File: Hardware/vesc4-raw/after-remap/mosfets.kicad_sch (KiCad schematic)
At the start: 15 parts, among them Q1 IRFS7530, Q2 IRFS7530, Q3 IRFS7530, Q4 IRFS7530, Q5 IRFS7530, Q6 IRFS7530

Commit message: export footprint & ngapus warning unmatched
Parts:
- Q1: symbol after-remap-rescue:MOSFET_N -> vesc4-legacy:MOSFET_N_8
- Q2: symbol after-remap-rescue:MOSFET_N -> vesc4-legacy:MOSFET_N_7
- Q3: symbol after-remap-rescue:MOSFET_N -> vesc4-legacy:MOSFET_N_11
- Q4: symbol after-remap-rescue:MOSFET_N -> vesc4-legacy:MOSFET_N_10
- Q5: symbol after-remap-rescue:MOSFET_N -> vesc4-legacy:MOSFET_N_12
- Q6: symbol after-remap-rescue:MOSFET_N -> vesc4-legacy:MOSFET_N_9
- R28: symbol after-remap-rescue:R-RESCUE-BLDC_4 -> vesc4-legacy:R-RESCUE-BLDC_4_13
- R29: symbol after-remap-rescue:R-RESCUE-BLDC_4 -> vesc4-legacy:R-RESCUE-BLDC_4_11
- R30: symbol after-remap-rescue:R-RESCUE-BLDC_4 -> vesc4-legacy:R-RESCUE-BLDC_4_10
- R34: symbol after-remap-rescue:R-RESCUE-BLDC_4 -> vesc4-legacy:R-RESCUE-BLDC_4_12
- R35: symbol after-remap-rescue:R-RESCUE-BLDC_4 -> vesc4-legacy:R-RESCUE-BLDC_4_15
- R36: symbol after-remap-rescue:R-RESCUE-BLDC_4 -> vesc4-legacy:R-RESCUE-BLDC_4_14
- R42: symbol after-remap-rescue:R-RESCUE-BLDC_4 -> vesc4-legacy:R-RESCUE-BLDC_4_18
- R43: symbol after-remap-rescue:R-RESCUE-BLDC_4 -> vesc4-legacy:R-RESCUE-BLDC_4_16
- R46: symbol after-remap-rescue:R-RESCUE-BLDC_4 -> vesc4-legacy:R-RESCUE-BLDC_4_17
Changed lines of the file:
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@@
 	(symbol
 		(lib_name "R-RESCUE-BLDC_4_17")
-		(lib_id "after-remap-rescue:R-RESCUE-BLDC_4")
+		(lib_id "vesc4-legacy:R-RESCUE-BLDC_4_17")
 		(at 199.39 102.87 270)
 		(unit 1)
@@
 	(symbol
 		(lib_name "R-RESCUE-BLDC_4_10")
-		(lib_id "after-remap-rescue:R-RESCUE-BLDC_4")
+		(lib_id "vesc4-legacy:R-RESCUE-BLDC_4_10")
 		(at 119.38 102.87 270)
 		(unit 1)
@@
 	(symbol
 		(lib_name "MOSFET_N_8")
-		(lib_id "after-remap-rescue:MOSFET_N")
+		(lib_id "vesc4-legacy:MOSFET_N_8")
 		(at 125.73 71.12 0)
 		(unit 1)
@@
 	(symbol
 		(lib_name "MOSFET_N_7")
-		(lib_id "after-remap-rescue:MOSFET_N")
+		(lib_id "vesc4-legacy:MOSFET_N_7")
 		(at 125.73 95.25 0)
 		(unit 1)
@@
 	(symbol
 		(lib_name "R-RESCUE-BLDC_4_11")
-		(lib_id "after-remap-rescue:R-RESCUE-BLDC_4")
+		(lib_id "vesc4-legacy:R-RESCUE-BLDC_4_11")
 		(at 111.76 95.25 270)
 		(unit 1)
@@
 	(symbol
 		(lib_name "R-RESCUE-BLDC_4_13")
-		(lib_id "after-remap-rescue:R-RESCUE-BLDC_4")
+		(lib_id "vesc4-legacy:R-RESCUE-BLDC_4_13")
 		(at 111.76 71.12 270)
 		(unit 1)
@@
 	(symbol
 		(lib_name "R-RESCUE-BLDC_4_12")
-		(lib_id "after-remap-rescue:R-RESCUE-BLDC_4")
+		(lib_id "vesc4-legacy:R-RESCUE-BLDC_4_12")
 		(at 151.13 71.12 270)
 		(unit 1)
@@
 	(symbol
 		(lib_name "R-RESCUE-BLDC_4_15")
-		(lib_id "after-remap-rescue:R-RESCUE-BLDC_4")
+		(lib_id "vesc4-legacy:R-RESCUE-BLDC_4_15")
 		(at 151.13 95.25 270)
 		(unit 1)
@@
 	(symbol
 		(lib_name "MOSFET_N_10")
-		(lib_id "after-remap-rescue:MOSFET_N")
+		(lib_id "vesc4-legacy:MOSFET_N_10")
 		(at 165.1 95.25 0)
 		(unit 1)
@@
 	(symbol
 		(lib_name "MOSFET_N_11")
-		(lib_id "after-remap-rescue:MOSFET_N")
+		(lib_id "vesc4-legacy:MOSFET_N_11")
 		(at 165.1 71.12 0)
 		(unit 1)
@@
 	(symbol
 		(lib_name "MOSFET_N_12")
-		(lib_id "after-remap-rescue:MOSFET_N")
+		(lib_id "vesc4-legacy:MOSFET_N_12")
 		(at 205.74 71.12 0)
 		(unit 1)
@@
 	(symbol
 		(lib_name "MOSFET_N_9")
-		(lib_id "after-remap-rescue:MOSFET_N")
+		(lib_id "vesc4-legacy:MOSFET_N_9")
 		(at 205.74 95.25 0)
 		(unit 1)
@@
 	(symbol
 		(lib_name "R-RESCUE-BLDC_4_16")
-		(lib_id "after-remap-rescue:R-RESCUE-BLDC_4")
+		(lib_id "vesc4-legacy:R-RESCUE-BLDC_4_16")
 		(at 191.77 95.25 270)
 		(unit 1)
@@
 	(symbol
 		(lib_name "R-RESCUE-BLDC_4_18")
-		(lib_id "after-remap-rescue:R-RESCUE-BLDC_4")
+		(lib_id "vesc4-legacy:R-RESCUE-BLDC_4_18")
 		(at 191.77 71.12 270)
 		(unit 1)
@@
 	(symbol
 		(lib_name "R-RESCUE-BLDC_4_14")
-		(lib_id "after-remap-rescue:R-RESCUE-BLDC_4")
+		(lib_id "vesc4-legacy:R-RESCUE-BLDC_4_14")
 		(at 151.13 102.87 90)
 		(unit 1)

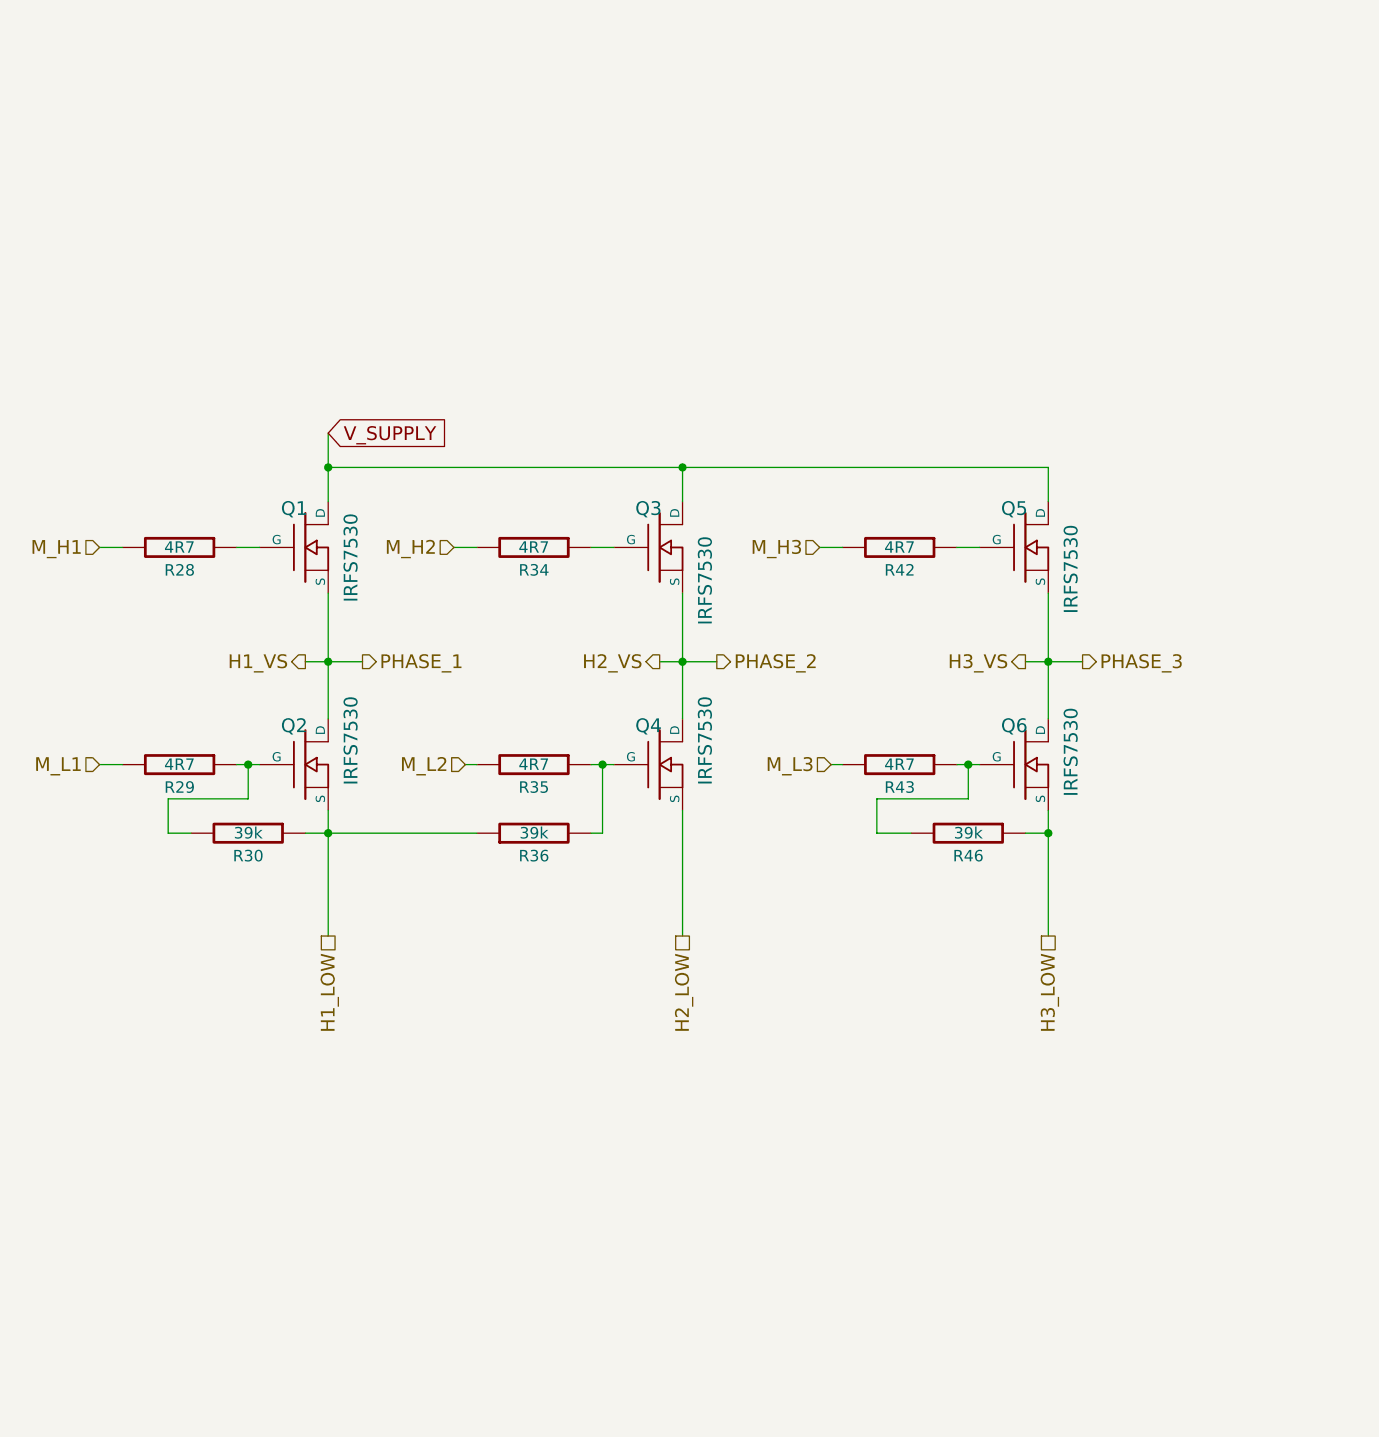
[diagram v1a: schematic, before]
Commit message: wiring mosfet baru
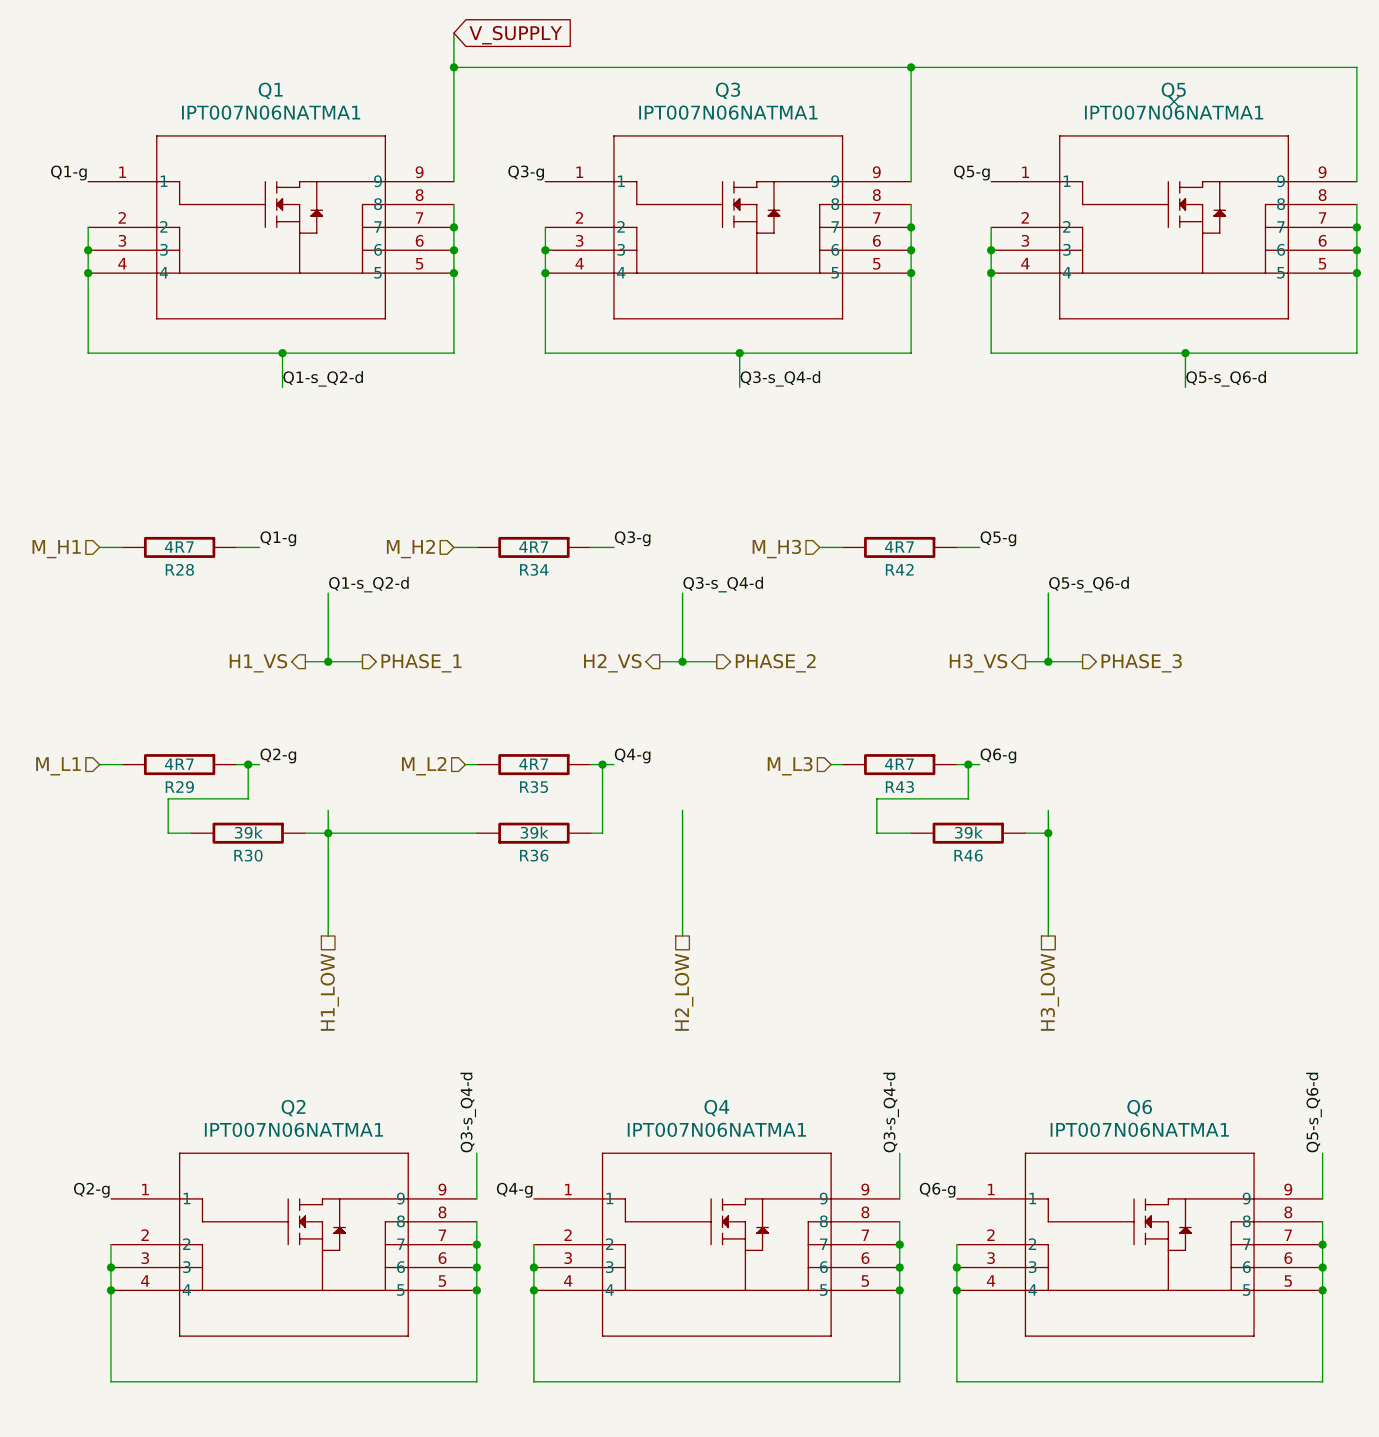
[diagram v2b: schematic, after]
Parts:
- removed Q1: IRFS7530, CRF1:D2PAK-7-GDS, symbol vesc4-legacy:MOSFET_N_8
- removed Q2: IRFS7530, CRF1:D2PAK-7-GDS, symbol vesc4-legacy:MOSFET_N_7
- removed Q3: IRFS7530, CRF1:D2PAK-7-GDS, symbol vesc4-legacy:MOSFET_N_11
- removed Q4: IRFS7530, CRF1:D2PAK-7-GDS, symbol vesc4-legacy:MOSFET_N_10
- removed Q5: IRFS7530, CRF1:D2PAK-7-GDS, symbol vesc4-legacy:MOSFET_N_12
- removed Q6: IRFS7530, CRF1:D2PAK-7-GDS, symbol vesc4-legacy:MOSFET_N_9
- added Q1, Q2, Q3, Q4, Q5, Q6: IPT007N06NATMA1, TRANS_IPT007N06NATMA1_INF, symbol ipt007n06n:IPT007N06NATMA1
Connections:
- net H1_VS: now also Q1.2, Q1.3, Q1.4, Q1.5, Q1.6, Q1.7, Q1.8
- net H2_VS: now also Q2.9, Q3.2, Q3.3, Q3.4, Q3.5, Q3.6, Q3.7, Q3.8, Q4.9
- net H3_VS: now also Q5.2, Q5.3, Q5.4, Q5.5, Q5.6, Q5.7, Q5.8, Q6.9
- net V_SUPPLY: now also Q1.9, Q3.9, Q5.9
- net Q6-g: now reaches R43.1, R46.2
- net Q6-g: now also Q6.1
- net Q2-g: now reaches R29.1, R30.2
- net Q2-g: now also Q2.1
- net Q1-g: now reaches R28.1
- net Q1-g: now also Q1.1
- net Q3-g: now reaches R34.1
- net Q3-g: now also Q3.1
- net Q4-g: now reaches R35.1, R36.2
- net Q4-g: now also Q4.1
- net Q5-g: now reaches R42.1
- net Q5-g: now also Q5.1
- new net: Q2.2, Q2.3, Q2.4, Q2.5, Q2.6, Q2.7, Q2.8
- new net: Q6.2, Q6.3, Q6.4, Q6.5, Q6.6, Q6.7, Q6.8
- new net: Q4.2, Q4.3, Q4.4, Q4.5, Q4.6, Q4.7, Q4.8
- no-connect marks 0 -> 1

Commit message: rewired mosfet baru di schematic
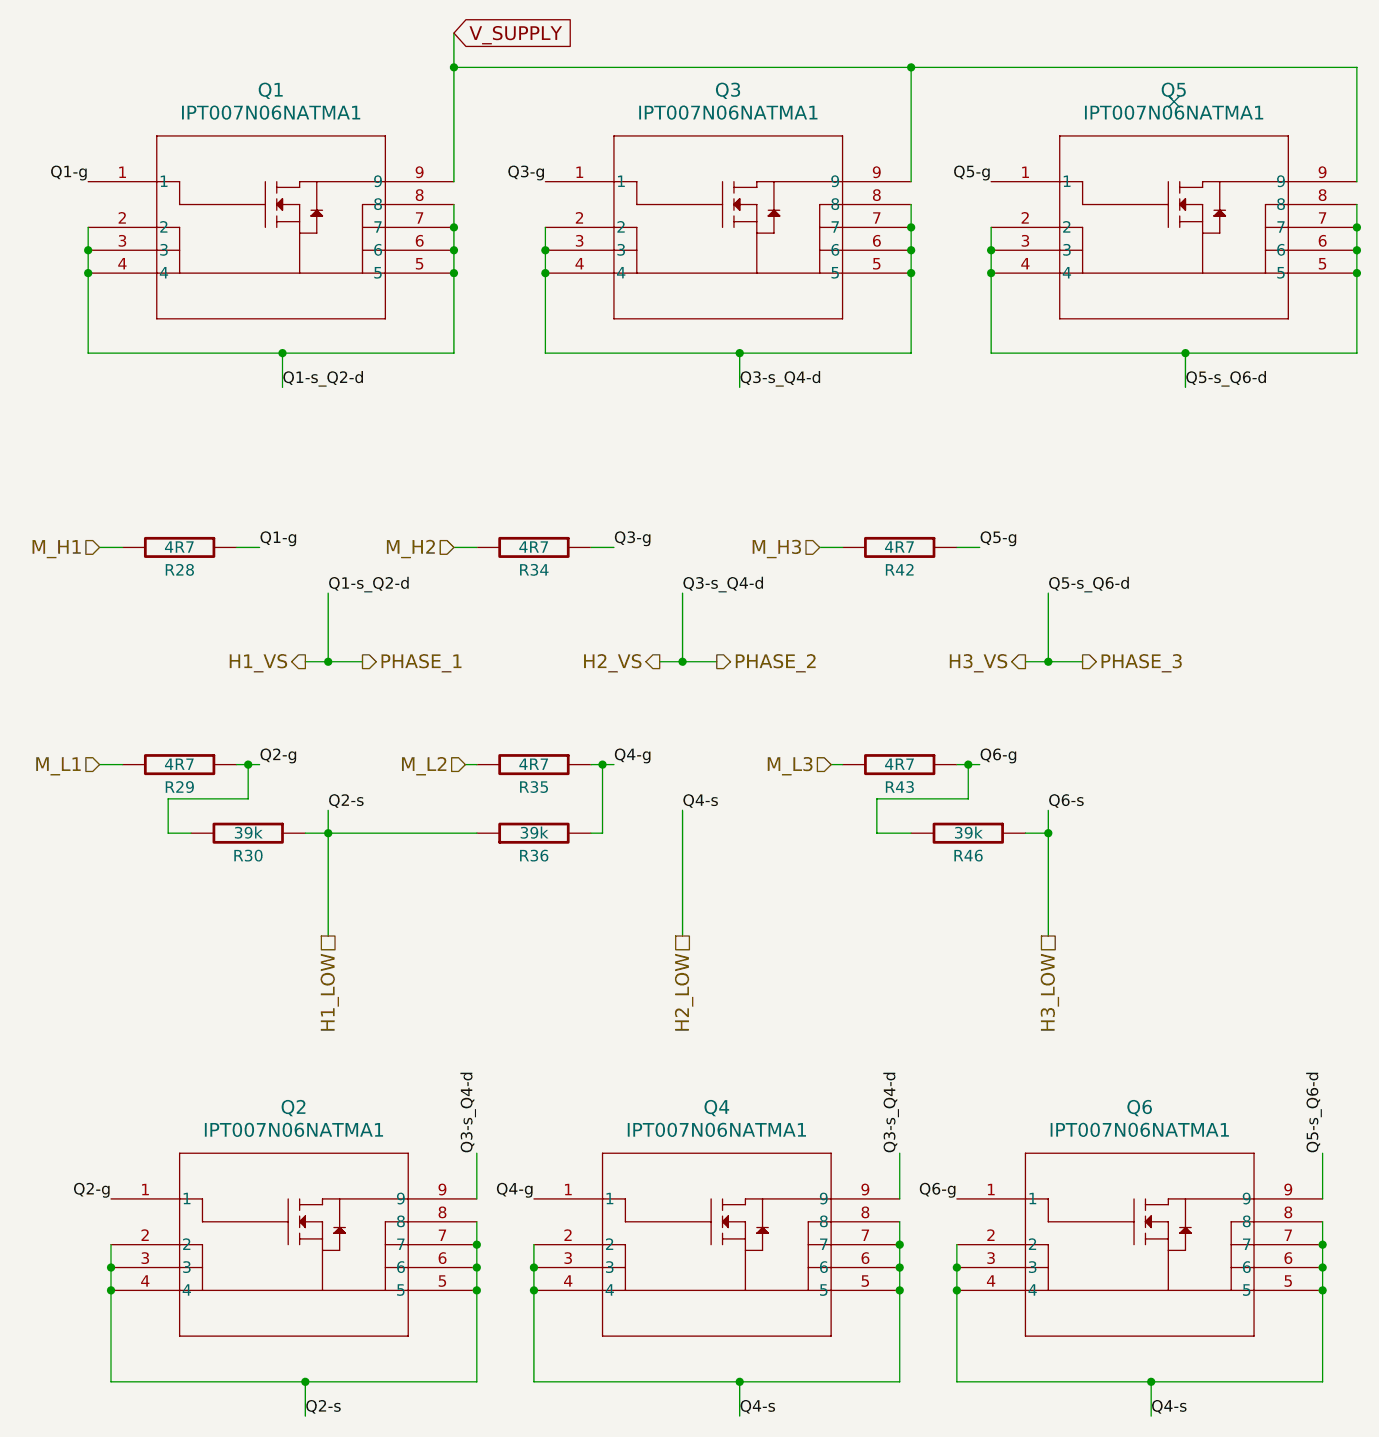
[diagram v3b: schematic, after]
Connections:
- net H1_LOW: now also Q2.2, Q2.3, Q2.4, Q2.5, Q2.6, Q2.7, Q2.8
- net H2_LOW: now also Q4.2, Q4.3, Q4.4, Q4.5, Q4.6, Q4.7, Q4.8, Q6.2, Q6.3, Q6.4, Q6.5, Q6.6, Q6.7, Q6.8
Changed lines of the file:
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@@
+	)
+	(junction
+		(at 125.73 163.83)
+		(diameter 0)
+		(color 0 0 0 0)
 	)
 	(junction
@@
 	)
 	(junction
+		(at 173.99 163.83)
+		(diameter 0)
+		(color 0 0 0 0)
+	)
+	(junction
 		(at 238.76 148.59)
 		(diameter 0)
@@
 	(junction
 		(at 191.77 151.13)
+		(diameter 0)
+		(color 0 0 0 0)
+	)
+	(junction
+		(at 219.71 163.83)
 		(diameter 0)
 		(color 0 0 0 0)
@@
 	(wire
 		(pts
+			(xy 125.73 163.83) (xy 104.14 163.83)
+		)
+		(stroke
+			(width 0)
+			(type default)
+		)
+	)
+	(wire
+		(pts
+			(xy 125.73 163.83) (xy 125.73 167.64)
+		)
+		(stroke
+			(width 0)
+			(type default)
+		)
+	)
+	(wire
+		(pts
 			(xy 102.87 95.25) (xy 105.41 95.25)
 		)
@@
 	(wire
 		(pts
-			(xy 198.12 163.83) (xy 238.76 163.83)
+			(xy 198.12 163.83) (xy 219.71 163.83)
 		)
 		(stroke
@@
 	(wire
 		(pts
+			(xy 173.99 163.83) (xy 173.99 167.64)
+		)
+		(stroke
+			(width 0)
+			(type default)
+		)
+	)
+	(wire
+		(pts
 			(xy 101.6 40.64) (xy 101.6 49.53)
 		)
@@
 	(wire
 		(pts
+			(xy 219.71 163.83) (xy 219.71 167.64)
+		)
+		(stroke
+			(width 0)
+			(type default)
+		)
+	)
+	(wire
+		(pts
 			(xy 199.39 95.25) (xy 199.39 99.06)
 		)
@@
 	(wire
 		(pts
-			(xy 151.13 163.83) (xy 191.77 163.83)
+			(xy 151.13 163.83) (xy 173.99 163.83)
 		)
 		(stroke
@@
 	(wire
 		(pts
-			(xy 144.78 163.83) (xy 104.14 163.83)
+			(xy 144.78 163.83) (xy 125.73 163.83)
 		)
 		(stroke
@@
 		(pts
 			(xy 191.77 151.13) (xy 191.77 148.59)
+		)
+		(stroke
+			(width 0)
+			(type default)
+		)
+	)
+	(wire
+		(pts
+			(xy 173.99 163.83) (xy 191.77 163.83)
+		)
+		(stroke
+			(width 0)
+			(type default)
+		)
+	)
+	(wire
+		(pts
+			(xy 219.71 163.83) (xy 238.76 163.83)
 		)
 		(stroke
@@
 		)
 	)
-	(label "Q3-s_Q4-d"
-		(at 167.64 76.2 0)
+	(label "Q2-s"
+		(at 128.27 100.33 0)
 		(effects
 			(font
@@
 		)
 	)
-	(label "Q1-s_Q2-d"
-		(at 123.19 53.34 0)
+	(label "Q4-s"
+		(at 167.64 100.33 0)
 		(effects
 			(font
@@
 		)
 	)
+	(label "Q3-s_Q4-d"
+		(at 167.64 76.2 0)
+		(effects
+			(font
+				(size 1.27 1.27)
+			)
+			(justify left bottom)
+		)
+	)
+	(label "Q1-s_Q2-d"
+		(at 123.19 53.34 0)
+		(effects
+			(font
+				(size 1.27 1.27)
+			)
+			(justify left bottom)
+		)
+	)
 	(label "Q1-g"
 		(at 101.6 30.48 180)
@@
 		)
 	)
-	(label "Q1-s_Q2-d"
-		(at 128.27 76.2 0)
+	(label "Q2-s"
+		(at 125.73 167.64 0)
 		(effects
 			(font
@@
 		)
 	)
-	(label "Q6-g"
-		(at 200.66 95.25 0)
+	(label "Q1-s_Q2-d"
+		(at 128.27 76.2 0)
 		(effects
 			(font
@@
 		)
 	)
+	(label "Q6-g"
+		(at 200.66 95.25 0)
+		(effects
+			(font
+				(size 1.27 1.27)
+			)
+			(justify left bottom)
+		)
+	)
+	(label "Q4-s"
+		(at 173.99 167.64 0)
+		(effects
+			(font
+				(size 1.27 1.27)
+			)
+			(justify left bottom)
+		)
+	)
 	(label "Q2-g"
 		(at 104.14 143.51 180)
@@
 		)
 	)
-	(label "Q3-s_Q4-d"
-		(at 144.78 138.43 90)
+	(label "Q6-s"
+		(at 208.28 100.33 0)
 		(effects
 			(font
@@
 	)
 	(label "Q3-s_Q4-d"
-		(at 173.99 53.34 0)
+		(at 144.78 138.43 90)
 		(effects
 			(font
@@
 		)
 	)
-	(label "Q2-g"
-		(at 120.65 95.25 0)
+	(label "Q3-s_Q4-d"
+		(at 173.99 53.34 0)
 		(effects
 			(font
@@
 		)
 	)
+	(label "Q2-g"
+		(at 120.65 95.25 0)
+		(effects
+			(font
+				(size 1.27 1.27)
+			)
+			(justify left bottom)
+		)
+	)
 	(label "Q1-g"
 		(at 120.65 71.12 0)
 		(effects
 			(font
+				(size 1.27 1.27)
+			)
+			(justify left bottom)
+		)
+	)
+	(label "Q4-s"
+		(at 219.71 167.64 0)
+		(effects
+			(font

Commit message: changed mosfet footprint jadi M
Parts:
- Q1, Q2, Q3, Q4, Q5, Q6: footprint TRANS_IPT007N06NATMA1_INF -> footprints:TRANS_IPT007N06NATMA1_INF-M
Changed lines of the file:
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@@
 			)
 		)
-		(property "Footprint" "TRANS_IPT007N06NATMA1_INF"
+		(property "Footprint" "footprints:TRANS_IPT007N06NATMA1_INF-M"
 			(at 101.6 30.48 0)
 			(effects
@@
 			)
 		)
-		(property "Footprint" "TRANS_IPT007N06NATMA1_INF"
+		(property "Footprint" "footprints:TRANS_IPT007N06NATMA1_INF-M"
 			(at 201.93 30.48 0)
 			(effects
@@
 			)
 		)
-		(property "Footprint" "TRANS_IPT007N06NATMA1_INF"
+		(property "Footprint" "footprints:TRANS_IPT007N06NATMA1_INF-M"
 			(at 104.14 143.51 0)
 			(effects
@@
 			)
 		)
-		(property "Footprint" "TRANS_IPT007N06NATMA1_INF"
+		(property "Footprint" "footprints:TRANS_IPT007N06NATMA1_INF-M"
 			(at 198.12 143.51 0)
 			(effects
@@
 			)
 		)
-		(property "Footprint" "TRANS_IPT007N06NATMA1_INF"
+		(property "Footprint" "footprints:TRANS_IPT007N06NATMA1_INF-M"
 			(at 151.13 143.51 0)
 			(effects
@@
 			)
 		)
-		(property "Footprint" "TRANS_IPT007N06NATMA1_INF"
+		(property "Footprint" "footprints:TRANS_IPT007N06NATMA1_INF-M"
 			(at 152.4 30.48 0)
 			(effects

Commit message: taro mosfet phase 1
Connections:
- net H1_VS: now also Q2.9
- net H2_VS: no longer Q2.9
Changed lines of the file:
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@@
 		)
 	)
-	(label "Q3-s_Q4-d"
+	(label "Q1-s_Q2-d"
 		(at 144.78 138.43 90)
 		(effects
